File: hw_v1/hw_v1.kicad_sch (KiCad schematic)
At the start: 0 parts

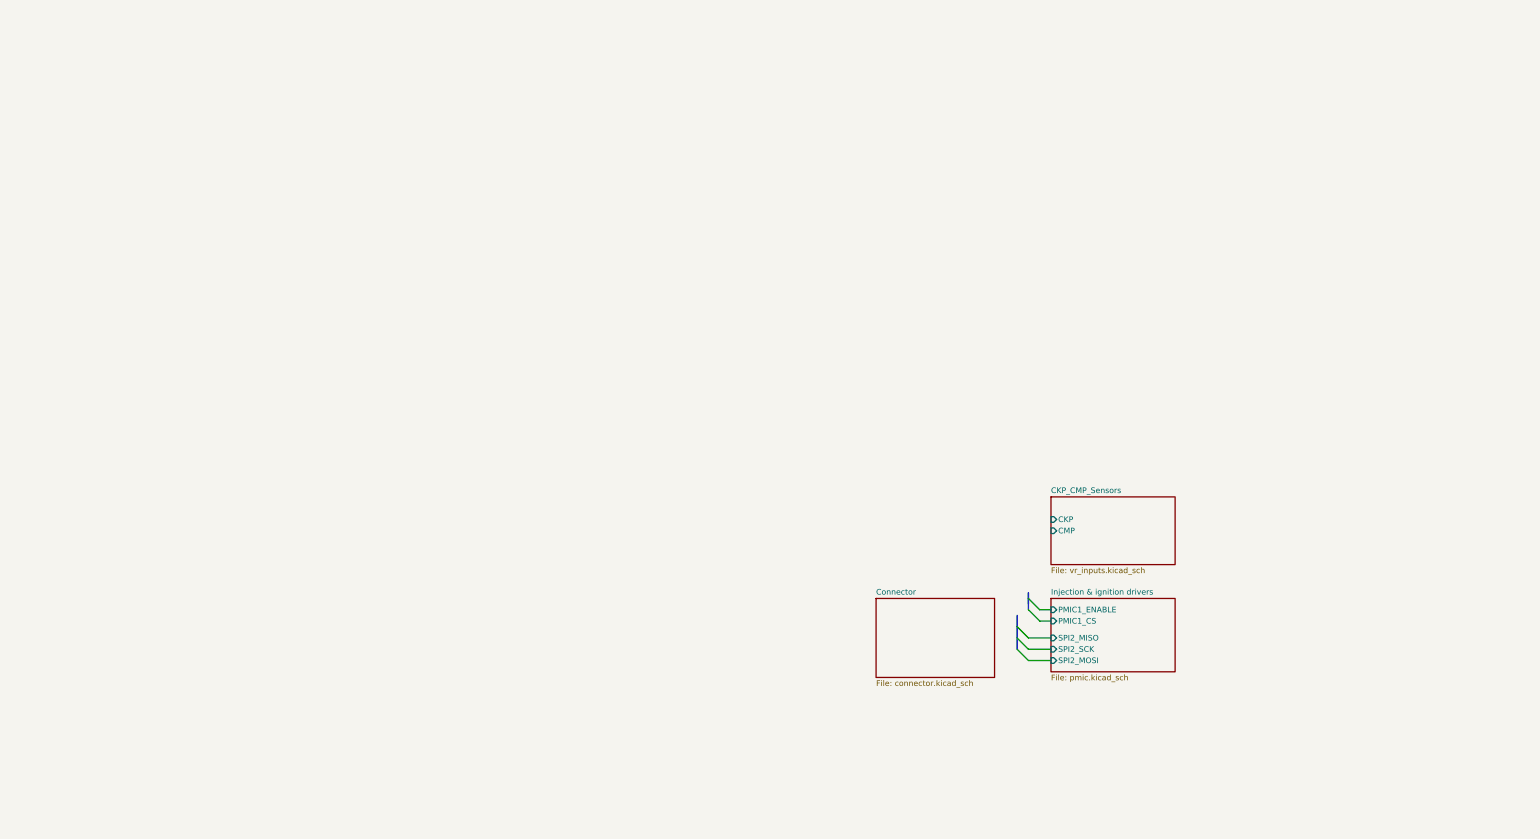
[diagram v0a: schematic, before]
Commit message: add sensors/ relay ouputs, connect all IO to mcu
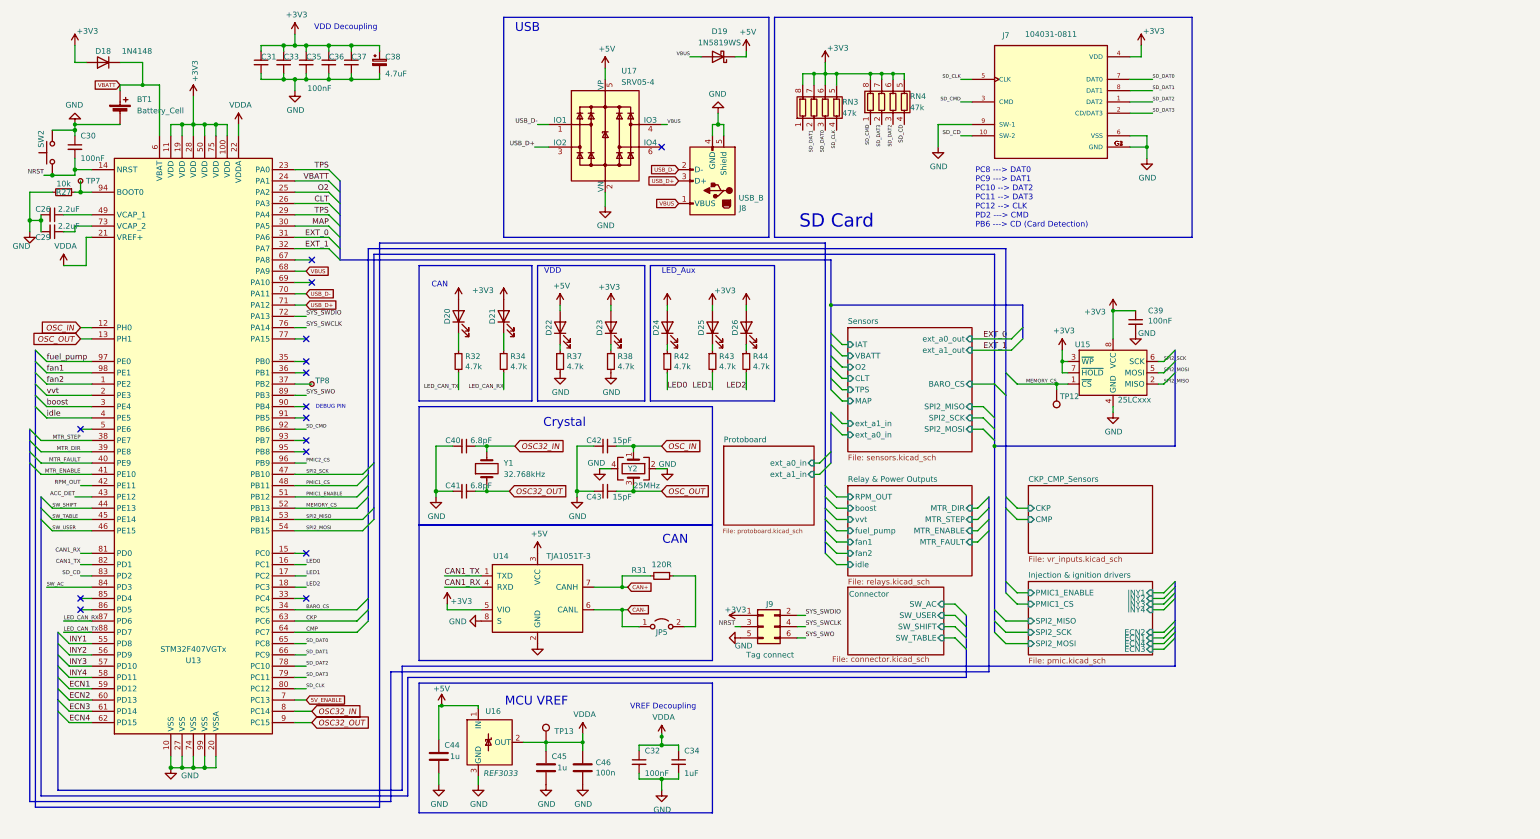
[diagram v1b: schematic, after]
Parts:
- added BT1: Battery_Cell, Connector_JST:JST_EH_B2B-EH-A_1x02_P2.50mm_Vertical, symbol Device:Battery_Cell
- added C26, C29: 2.2uF, Capacitor_SMD:C_0805_2012Metric, symbol Device:C_Small
- added C30, C31, C32, C33, C35, C36, C37, C39: 100nF, Capacitor_SMD:C_0805_2012Metric, symbol Device:C_Small
- added C34: 1uF, Capacitor_SMD:C_0805_2012Metric, symbol Device:C_Small
- added C38: 4.7uF, Capacitor_SMD:C_0805_2012Metric, symbol Device:CP_Small
- added C40, C41: 6.8pF, Capacitor_SMD:C_0805_2012Metric, symbol Device:C_Small
- added C42, C43: 15pF, Capacitor_SMD:C_0805_2012Metric, symbol Device:C_Small
- added C44, C45: 1u, Capacitor_SMD:C_0402_1005Metric, symbol Device:C
- added C46: 100n, Capacitor_SMD:C_0402_1005Metric, symbol Device:C
- added D18: 1N4148, Diode_SMD:D_SOD-523, symbol Diode:1N4148
- added D19: 1N5819WS, Diode_SMD:D_SOD-323_HandSoldering, symbol Diode:SB160
- added D20, D21, D22, D23, D24, D25, D26: LED, LED_SMD:LED_0805_2012Metric, symbol Device:LED
- added J7: 104031-0811, Library:MOLEX_104031-0811, symbol Library:104031-0811
- added J8: USB_B, Connector_USB:USB_Mini-B_Tensility_54-00023_Vertical, symbol STM32F_rev3-rescue:USB_B-Connector
- added J9: Tag connect, Connector:Tag-Connect_TC2030-IDC-FP_2x03_P1.27mm_Vertical, symbol Connector_Generic:Conn_02x03_Odd_Even
- added JP5: Jumper_2_Open, Jumper:SolderJumper-2_P1.3mm_Bridged2Bar_Pad1.0x1.5mm, symbol Jumper:Jumper_2_Open
- added R27: 10k, Resistor_SMD:R_0603_1608Metric, symbol Device:R_Small
- added R31: 120R, Resistor_SMD:R_1206_3216Metric, symbol Device:R_Small
- added R32, R34, R37, R38, R42, R43, R44: 4.7k, Resistor_SMD:R_0603_1608Metric, symbol Device:R_Small
- added RN3, RN4: 47k, Resistor_SMD:R_Array_Convex_4x0603, symbol Device:R_Pack04
- added SW2: SW_Push, Button_Switch_SMD:SW_SPST_TL3342, symbol Switch:SW_Push
- added TP12, TP13: TestPoint, TestPoint:TestPoint_Pad_1.0x1.0mm, symbol Connector:TestPoint
- added TP7: BOOT0, TestPoint:TestPoint_Pad_D2.0mm, symbol Connector:TestPoint_Small
- added TP8: BOOT1, TestPoint:TestPoint_Pad_D2.0mm, symbol Connector:TestPoint_Small
- added U13: STM32F407VGTx, Package_QFP:LQFP-100_14x14mm_P0.5mm, symbol MCU_ST_STM32F4:STM32F407VGTx
- added U14: TJA1051T-3, Package_SO:SOP-8_3.9x4.9mm_P1.27mm, symbol Interface_CAN_LIN:TJA1051T-3
- added U15: 25LCxxx, Package_SO:SOIC-8_5.275x5.275mm_P1.27mm, symbol Memory_EEPROM:25LCxxx
- added U16: REF3033, Package_TO_SOT_SMD:SOT-23, symbol Reference_Voltage:REF3033
- added U17: SRV05-4, Package_TO_SOT_SMD:SOT-23-6, symbol Power_Protection:SRV05-4
- added Y1: 32.768kHz, Crystal:Crystal_SMD_2012-2Pin_2.0x1.2mm, symbol Device:Crystal
- added Y2: 25MHz, Crystal:Crystal_SMD_3225-4Pin_3.2x2.5mm, symbol Device:Crystal_GND24
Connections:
- new net: C26.1, U13.49 (VCAP_1)
- new net: D22.1 (K), R37.1
- new net: JP5.2 (B), R31.1
- new net: D26.1 (K), R44.1
- new net: C29.1, U13.73 (VCAP_2)
- new net: TP8.1, U13.37 (PB2)
- new net: D21.1 (K), R34.1
- new net: D20.1 (K), R32.1
- new net: D25.1 (K), R43.1
- new net: R27.1, TP7.1, U13.94 (BOOT0)
- new net: D24.1 (K), R42.1
- new net: D23.1 (K), R38.1
- new net +3V3: C31.1, C33.1, C35.1, C36.1, C37.1, C38.1, C39.1, D18.2 (A), D20.2 (A), D21.2 (A), D23.2 (A), D24.2 (A), D25.2 (A), D26.2 (A), J7.4 (VDD), J9.1 (Pin_1), RN3.5 (R4.2), RN3.6 (R3.2), RN3.7 (R2.2), RN3.8 (R1.2), RN4.5 (R4.2), RN4.6 (R3.2), RN4.7 (R2.2), RN4.8 (R1.2), U13.100 (VDD), U13.11 (VDD), U13.19 (VDD), U13.28 (VDD), U13.50 (VDD), U13.75 (VDD), U14.5 (VIO), U15.3 (~{WP}), U15.7 (~{HOLD}), U15.8 (VCC)
- new net +5V: C44.1, D19.1 (K), D22.2 (A), U14.3 (VCC), U16.1 (IN), U17.5 (VP)
- new net 5V_ENABLE: U13.7 (PC13)
- new net ACC_DET: U13.43 (PE12)
- new net BARO_CS: U13.34 (PC5)
- new net CAN+: R31.2, U14.7 (CANH)
- new net CAN-: JP5.1 (A), U14.6 (CANL)
- new net CAN1_RX: U13.81 (PD0), U14.4 (RXD)
- new net CAN1_TX: U13.82 (PD1), U14.1 (TXD)
- new net CKP: U13.63 (PC6)
- new net CLT: U13.26 (PA3)
- new net CMP: U13.64 (PC7)
- new net ECN1: U13.59 (PD12)
- new net ECN2: U13.60 (PD13)
- new net ECN3: U13.61 (PD14)
- new net ECN4: U13.62 (PD15)
- new net EXT_0: U13.31 (PA6)
- new net EXT_1: U13.32 (PA7)
- new net GND: BT1.2 (-), C26.2, C29.2, C30.1, C31.2, C32.2, C33.2, C34.2, C35.2, C36.2, C37.2, C38.2, C39.2, C40.2, C41.2, C42.2, C43.2, C44.2, C45.2, C46.2, J7.6 (VSS), J7.9 (SW-1), J7.G1 (GND), J7.G2 (GND), J7.G3 (GND), J7.G4 (GND), J8.4 (GND), J8.5 (Shield), J9.5 (Pin_5), R27.2, R37.2, R38.2, SW2.2, U13.10 (VSS), U13.20 (VSSA), U13.27 (VSS), U13.74 (VSS), U13.99 (VSS), U14.2 (GND), U14.8 (S), U15.4 (GND), U16.3 (GND), U17.2 (VN), Y2.2, Y2.4
- new net INY1: U13.55 (PD8)
- new net INY2: U13.56 (PD9)
- new net INY3: U13.57 (PD10)
- new net INY4: U13.58 (PD11)
- new net LED0: R42.2, U13.16 (PC1)
- new net LED1: R43.2, U13.17 (PC2)
- new net LED2: R44.2, U13.18 (PC3)
- new net LED_CAN_RX: R34.2, U13.87 (PD6)
- new net LED_CAN_TX: R32.2, U13.88 (PD7)
- new net MAP: U13.30 (PA5)
- new net MEMORY_CS: TP12.1, U13.52 (PB13), U15.1 (~{CS})
- new net MTR_DIR: U13.39 (PE8)
- new net MTR_ENABLE: U13.41 (PE10)
- new net MTR_FAULT: U13.40 (PE9)
- new net MTR_STEP: U13.38 (PE7)
- new net NRST: C30.2, J9.3 (Pin_3), SW2.1, U13.14 (NRST)
- new net O2: U13.25 (PA2)
- new net OSC32_IN: C40.1, U13.8 (PC14), Y1.2
- new net OSC32_OUT: C41.1, U13.9 (PC15), Y1.1
- new net OSC_IN: C42.1, U13.12 (PH0), Y2.1
- new net OSC_OUT: C43.1, U13.13 (PH1), Y2.3
- new net PMIC1_CS: U13.48 (PB11)
- new net PMIC1_ENABLE: U13.51 (PB12)
- new net PMIC2_CS: U13.96 (PB9)
- new net RPM_OUT: U13.42 (PE11)
- new net SD_CD: J7.10 (SW-2), RN4.4 (R4.1), U13.83 (PD2)
- new net SD_CLK: J7.5 (CLK), RN3.4 (R4.1), U13.80 (PC12)
- new net SD_CMD: J7.3 (CMD), RN4.1 (R1.1), U13.92 (PB6)
- new net SD_DAT0: J7.7 (DAT0), RN3.3 (R3.1), U13.65 (PC8)
- new net SD_DAT1: J7.8 (DAT1), RN3.2 (R2.1), U13.66 (PC9)
- new net SD_DAT2: J7.1 (DAT2), RN4.3 (R3.1), U13.78 (PC10)
- new net SD_DAT3: J7.2 (CD/DAT3), RN4.2 (R2.1), U13.79 (PC11)
- new net SPI2_MISO: U13.53 (PB14), U15.2 (MISO)
- new net SPI2_MOSI: U13.54 (PB15), U15.5 (MOSI)
- new net SPI2_SCK: U13.47 (PB10), U15.6 (SCK)
- new net SW_AC: U13.84 (PD3)
- new net SW_SHIFT: U13.44 (PE13)
- new net SW_TABLE: U13.45 (PE14)
- new net SW_USER: U13.46 (PE15)
- new net SYS_SWCLK: J9.4 (Pin_4), U13.76 (PA14)
- new net SYS_SWDIO: J9.2 (Pin_2), U13.72 (PA13)
- new net SYS_SWO: J9.6 (Pin_6), U13.89 (PB3)
- new net TPS: U13.23 (PA0), U13.29 (PA4)
- new net USB_D+: J8.3 (D+), U13.71 (PA12), U17.3 (IO2)
- new net USB_D-: J8.2 (D-), U13.70 (PA11), U17.1 (IO1)
- new net VBATT: BT1.1 (+), D18.1 (K), U13.24 (PA1), U13.6 (VBAT)
- new net VBUS: D19.2 (A), J8.1 (VBUS), U13.68 (PA9), U17.4 (IO3)
- new net VDDA: C32.1, C34.1, C45.1, C46.1, TP13.1, U13.21 (VREF+), U13.22 (VDDA), U16.2 (OUT)
- new net boost: U13.3 (PE4)
- new net fan1: U13.98 (PE1)
- new net fan2: U13.1 (PE2)
- new net fuel_pump: U13.97 (PE0)
- new net idle: U13.4 (PE5)
- new net vvt: U13.2 (PE3)
- no-connect marks 0 -> 15
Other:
- added sheet Protoboard (protoboard.kicad_sch)
- added sheet Relay & Power Outputs (relays.kicad_sch)
- added sheet Sensors (sensors.kicad_sch)
- sheet Connector ports: added SW_AC, SW_SHIFT, SW_TABLE, SW_USER; removed none
- sheet Injection & ignition drivers ports: added ECN1, ECN2, ECN3, ECN4, INY1, INY2, INY3, INY4; removed none
- note added: "CAN"
- note added: "Crystal"
- note added: "DEBUG PIN"
- note added: "LED_Aux"
- note added: "MCU VREF"
- note added: "PC8 ---> DAT0 PC9 ---> DAT1 PC10 --> DAT2 PC11 --> DAT3 PC12 --> CLK PD2 ---> CMD PB6 ---> CD (Card Detection)"
- note added: "SD Card"
- note added: "USB"
- note added: "VDD"
- note added: "VDD Decoupling"
- note added: "VREF Decoupling"
- company: (none) -> Churrosoft ®
- title: (none) -> μEFI (Speeduino FW compatible)

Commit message: wip pcb layout
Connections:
- net LED_CAN_RX: now also U13.33 (PC4); no longer U13.87 (PD6)
- net SW_Clutch_m: now reaches U13.85 (PD4)
- net USART_2_TX: now reaches U13.86 (PD5)
- net ACCL_CS: now reaches U13.95 (PB8)
- net SW_AC renamed SW_AC_m
- net SW_SHIFT renamed SW_SHIFT_m
- net SW_TABLE renamed SW_TABLE_m
- net SW_USER renamed SW_USER_m
- new net USART_2_RX: U13.87 (PD6)
- no-connect marks 15 -> 11
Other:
- sheet Connector ports: added SW_AC_m, SW_Clutch_m, SW_SHIFT_m, SW_TABLE_m, SW_USER_m; removed SW_AC, SW_SHIFT, SW_TABLE, SW_USER
- sheet Sensors ports: added ACCL_CS; removed none
- note added: "PROTO 0/1"
- moved on the sheet: C32, C34, C39, C44, C45, C46, TP12, TP13, U15, U16

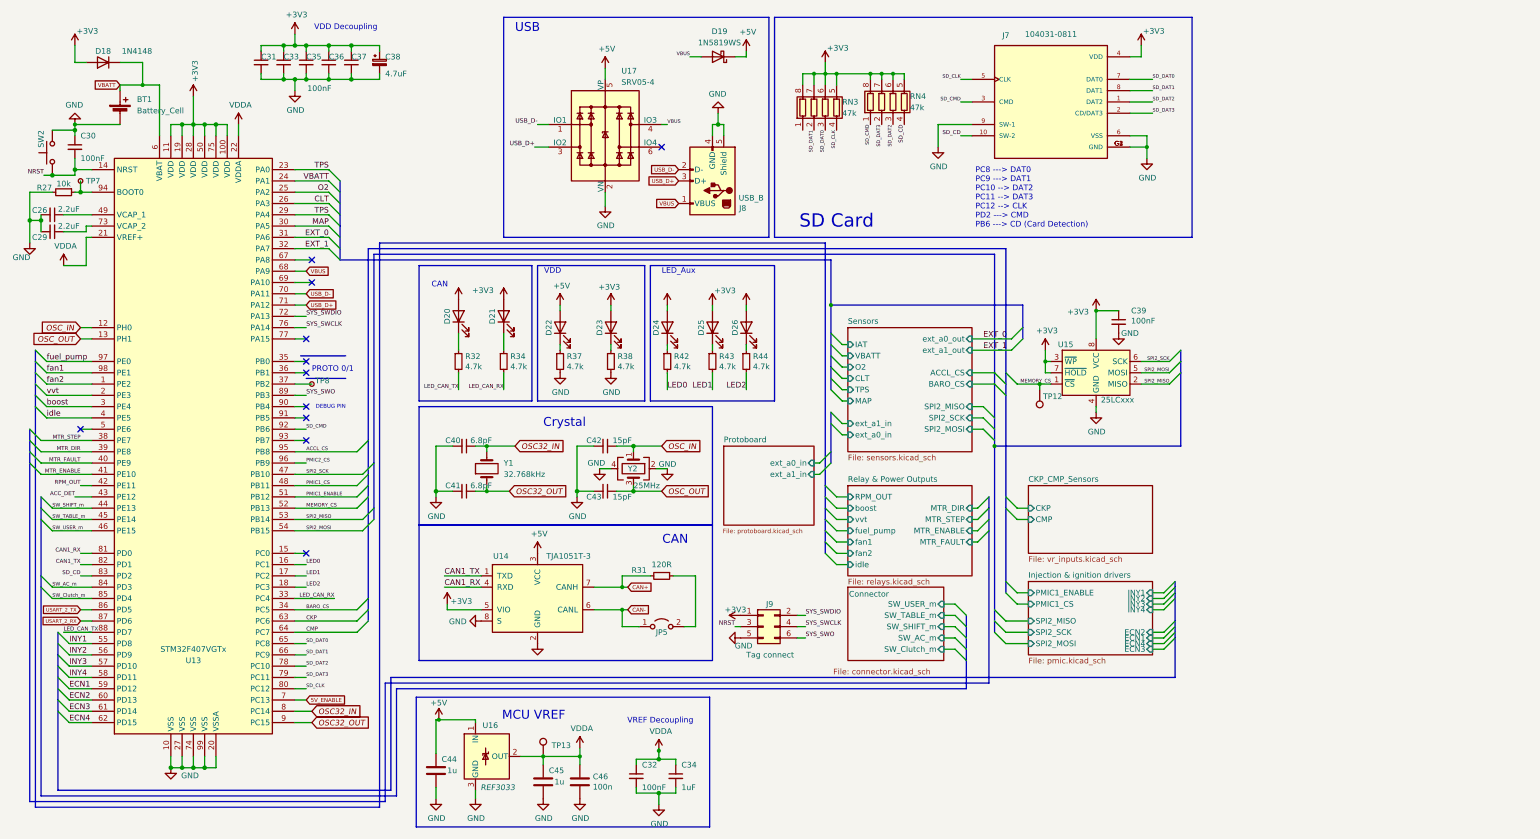
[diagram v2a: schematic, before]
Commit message: placed al SMD, wip pmic traces
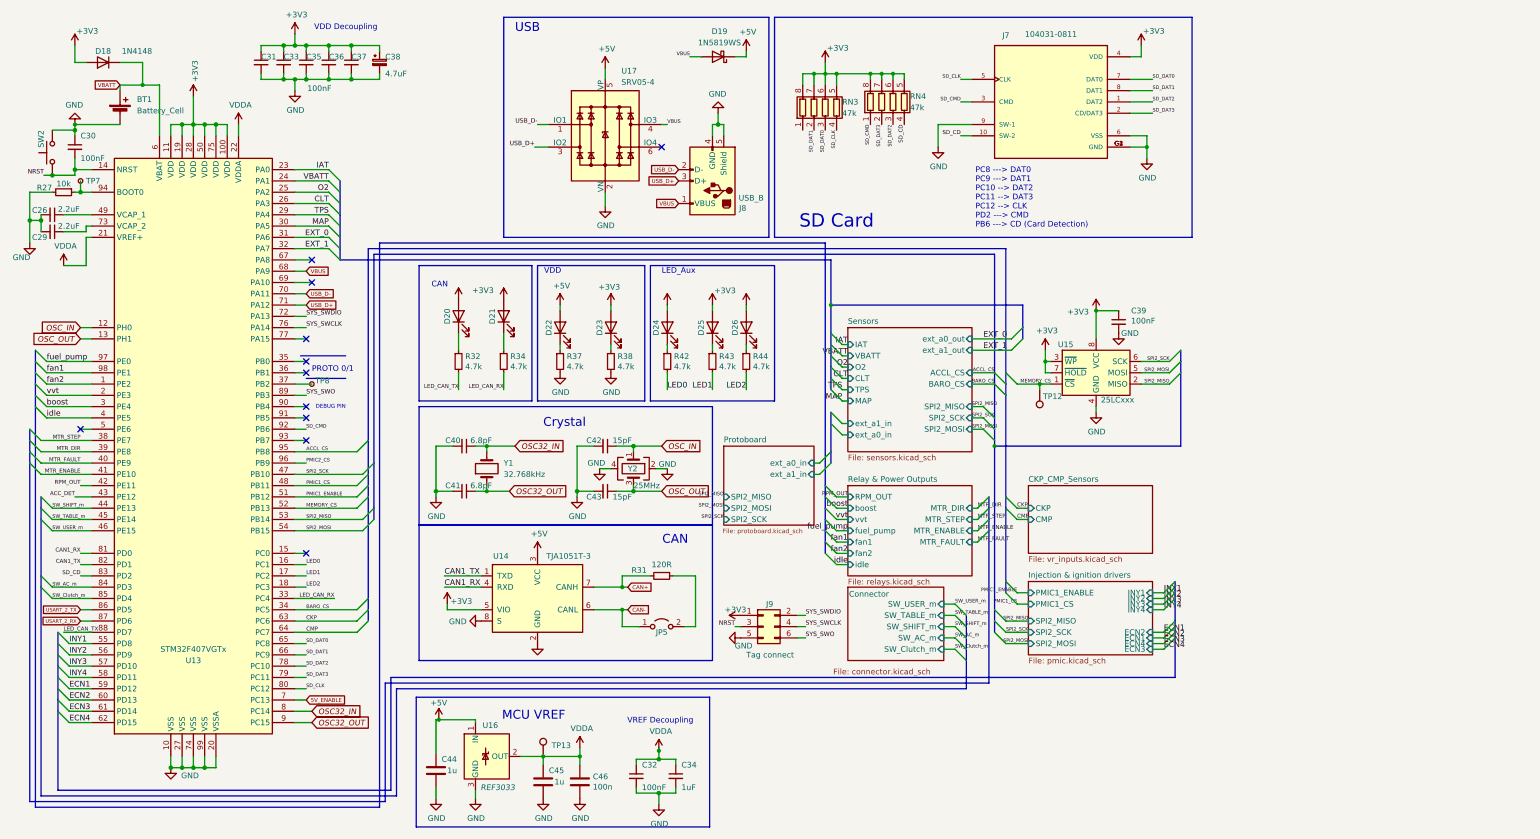
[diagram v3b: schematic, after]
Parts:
- J7: footprint Library:MOLEX_104031-0811 -> Connector_Card:microSD_HC_Molex_104031-0811
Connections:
- net TPS: no longer U13.23 (PA0)
- new net IAT: U13.23 (PA0)
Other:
- sheet Protoboard ports: added SPI2_MISO, SPI2_MOSI, SPI2_SCK; removed none
